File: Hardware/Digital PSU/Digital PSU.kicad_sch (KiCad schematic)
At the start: 35 parts, among them J1 ACin, J2 Relay power, J3 Conn_02x09, Q1 NJW0302, Q2 MJE15030, U1 LM334Z

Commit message: More work on PSU
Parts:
- R3: footprint Resistor_THT:R_Axial_DIN0207_L6.3mm_D2.5mm_P10.16mm_Horizontal -> Potentiometer_THT:Potentiometer_Bourns_3296W_Vertical; symbol Device:R_Variable -> Device:R_Potentiometer
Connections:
- net GND: now also R3.1; no longer R3.2
- net at D15.1 (K), J3.10 (Pin_10), J3.12 (Pin_12)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: now also R3.2, R3.3; no longer R3.1
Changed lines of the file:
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@@
+	(wire
+		(pts
+			(xy 102.616 153.162) (xy 96.012 153.162)
+		)
+		(stroke
+			(width 0)
+			(type default)
+		)
+	)
 	(wire
 		(pts
@@
 	(wire
 		(pts
+			(xy 96.012 153.162) (xy 96.012 158.496)
+		)
+		(stroke
+			(width 0)
+			(type default)
+		)
+	)
+	(wire
+		(pts
 			(xy 82.55 164.592) (xy 102.616 164.592)
 		)
@@
 		(pts
 			(xy 184.658 89.662) (xy 184.658 84.582)
+		)
+		(stroke
+			(width 0)
+			(type default)
+		)
+	)
+	(wire
+		(pts
+			(xy 96.012 158.496) (xy 98.806 158.496)
 		)
 		(stroke
@@
 	)
 	(symbol
-		(lib_id "Device:R_Variable")
-		(at 102.616 158.496 0)
+		(lib_id "Device:R_Potentiometer")
+		(at 102.616 158.496 180)
 		(unit 1)
 		(exclude_from_sim no)
@@
 		(fields_autoplaced yes)
 		(property "Reference" "R3"
-			(at 105.791 157.2838 0)
-			(effects
-				(font
-					(size 1.27 1.27)
-				)
-				(justify left)
+			(at 104.394 157.2838 0)
+			(effects
+				(font
+					(size 1.27 1.27)
+				)
+				(justify right)
 			)
 		)
 		(property "Value" "500R"
-			(at 105.791 159.7081 0)
-			(effects
-				(font
-					(size 1.27 1.27)
-				)
-				(justify left)
-			)
-		)
-		(property "Footprint" "Resistor_THT:R_Axial_DIN0207_L6.3mm_D2.5mm_P10.16mm_Horizontal"
-			(at 100.838 158.496 90)
+			(at 104.394 159.7081 0)
+			(effects
+				(font
+					(size 1.27 1.27)
+				)
+				(justify right)
+			)
+		)
+		(property "Footprint" "Potentiometer_THT:Potentiometer_Bourns_3296W_Vertical"
+			(at 102.616 158.496 0)
 			(effects
 				(font
@@
 			)
 		)
-		(property "Description" "Variable resistor"
+		(property "Description" "Potentiometer"
 			(at 102.616 158.496 0)
 			(effects
@@
 		(pin "1"
 		)
-		(instances
+		(pin "3"
+		)
+		(instances

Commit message: Added transformer for Digital PSU
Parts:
- added F2: Fuse - 8A T, ThePreAmp_PSU_Fuseholder:Keystone fuseholder 4527, symbol Device:Fuse
- added J4: 15V AC, THE_PREAMP_CONN_POWER_5_08:TBP01R1-508-02BK, symbol Connector:Conn_01x02_Socket
- added J5: 230V AC, THE_PREAMP_CONN_POWER_5_08:TBP01R1-508-02BK, symbol Connector:Conn_01x02_Socket
- added TR1: Hahn BV EL 603 1027, Transformer_Hahn_BV_EL_603_1027:Transformer_Hahn_BV_EL_603_1027, symbol Transformer_Hahn_BV_EL_603_1027:Hahn_BV_EL_603_1027
- J1: value ACin -> AC in
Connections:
- new net: F2.1, J5.1 (Pin_1)
- new net: J5.2 (Pin_2), TR1.7
- new net: J4.1 (Pin_1), TR1.9
- new net: J4.2 (Pin_2), TR1.13
- new net: F2.2, TR1.1

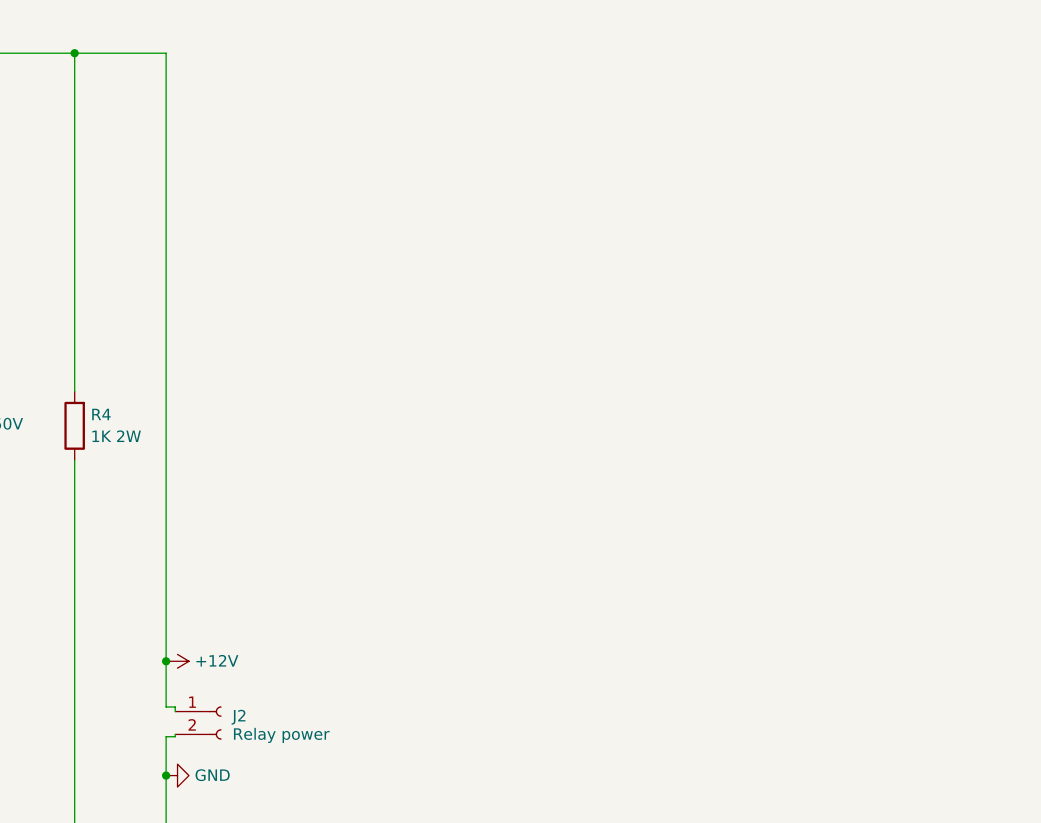
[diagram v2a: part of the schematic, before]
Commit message: Added LD1117V33 to digital psu
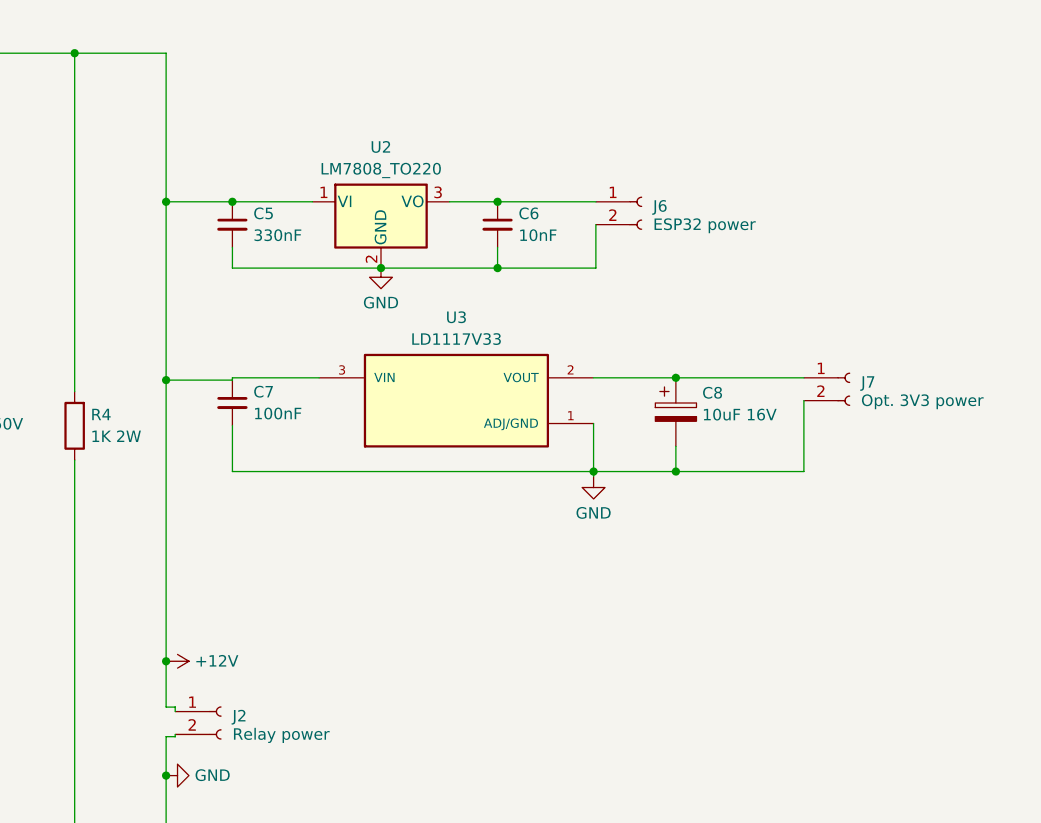
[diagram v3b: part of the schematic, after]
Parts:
- added C5: 330nF, symbol Device:C_Small
- added C6: 10nF, symbol Device:C_Small
- added C7: 100nF, symbol Device:C_Small
- added C8: 10uF 16V, Capacitor_THT:CP_Radial_D10.0mm_P5.00mm, symbol Device:C_Polarized
- added J6: ESP32 power, THE_PREAMP_CONN_POWER_5_08:TBP01R1-508-02BK, symbol Connector:Conn_01x02_Socket
- added J7: Opt. 3V3 power, THE_PREAMP_CONN_POWER_5_08:TBP01R1-508-02BK, symbol Connector:Conn_01x02_Socket
- added U2: LM7808_TO220, Package_TO_SOT_THT:TO-220-3_Vertical, symbol Regulator_Linear:LM7808_TO220
- added U3: LD1117V33, LD1117V33:TO255P1020X450X1968-3, symbol LD1117V33:LD1117V33
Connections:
- net +12V: now also C5.1, C7.1, U2.1 (VI), U3.3 (VIN)
- net GND: now also C5.2, C6.2, C7.2, C8.2, J6.2 (Pin_2), J7.2 (Pin_2), U2.2 (GND), U3.1 (ADJ/GND)
- new net: C8.1, J7.1 (Pin_1), U3.2 (VOUT)
- new net: C6.1, J6.1 (Pin_1), U2.3 (VO)

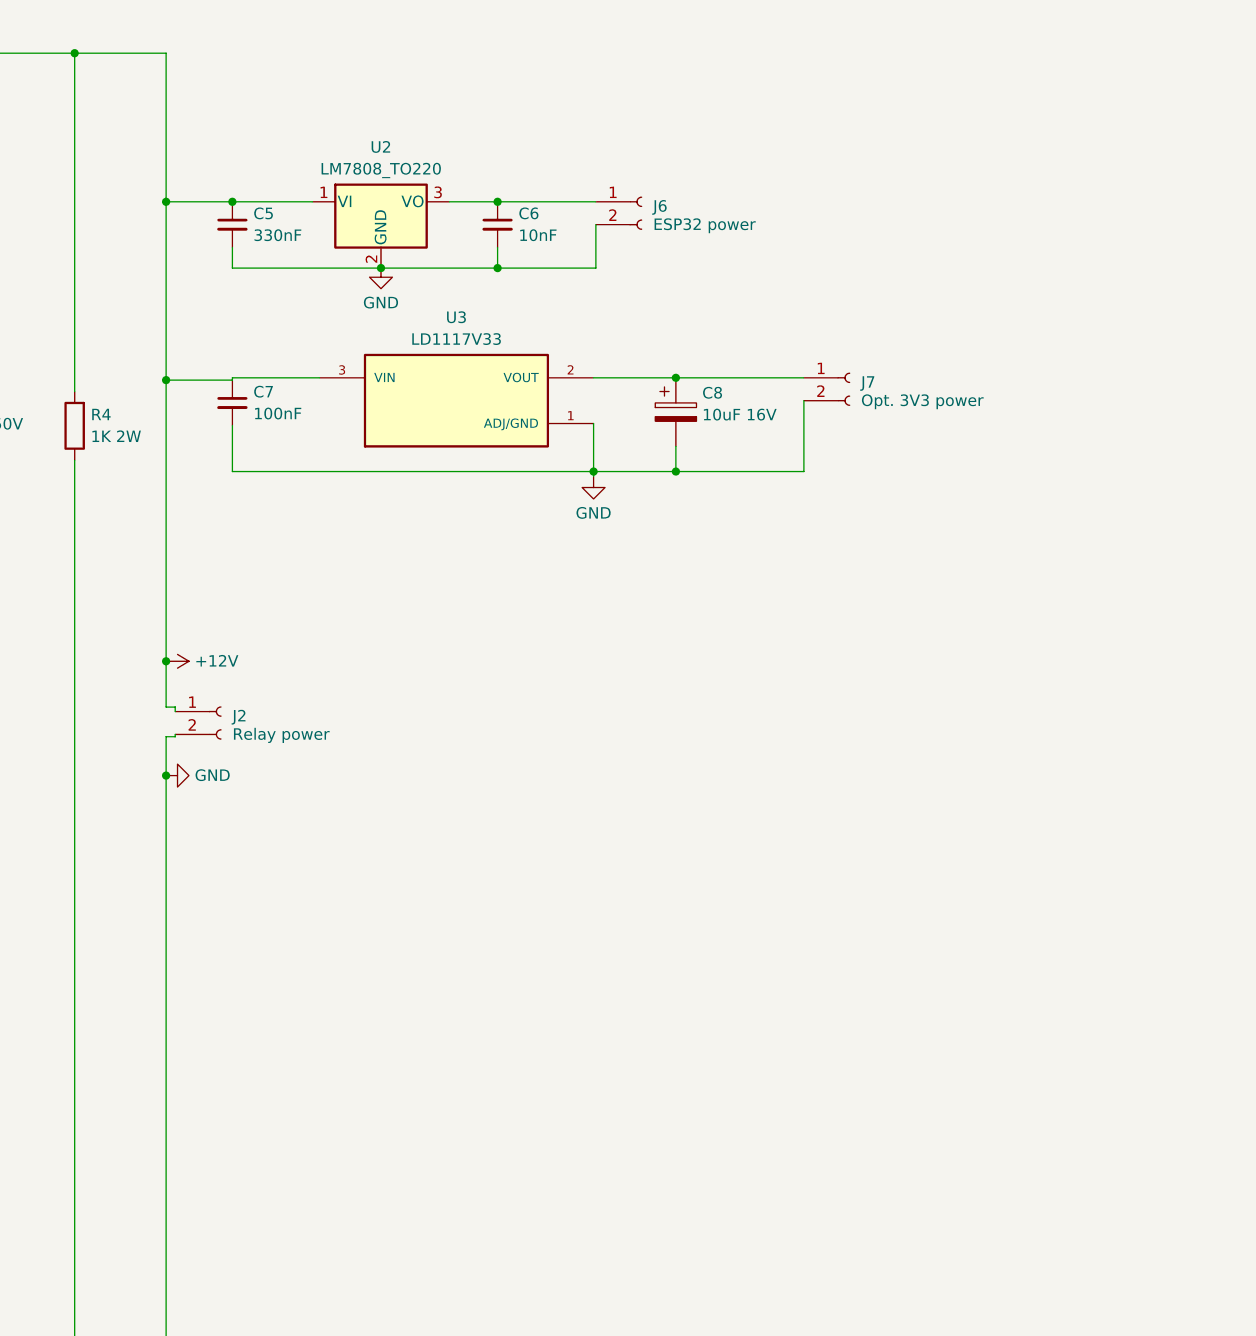
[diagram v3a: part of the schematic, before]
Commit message: Pcb dimensions
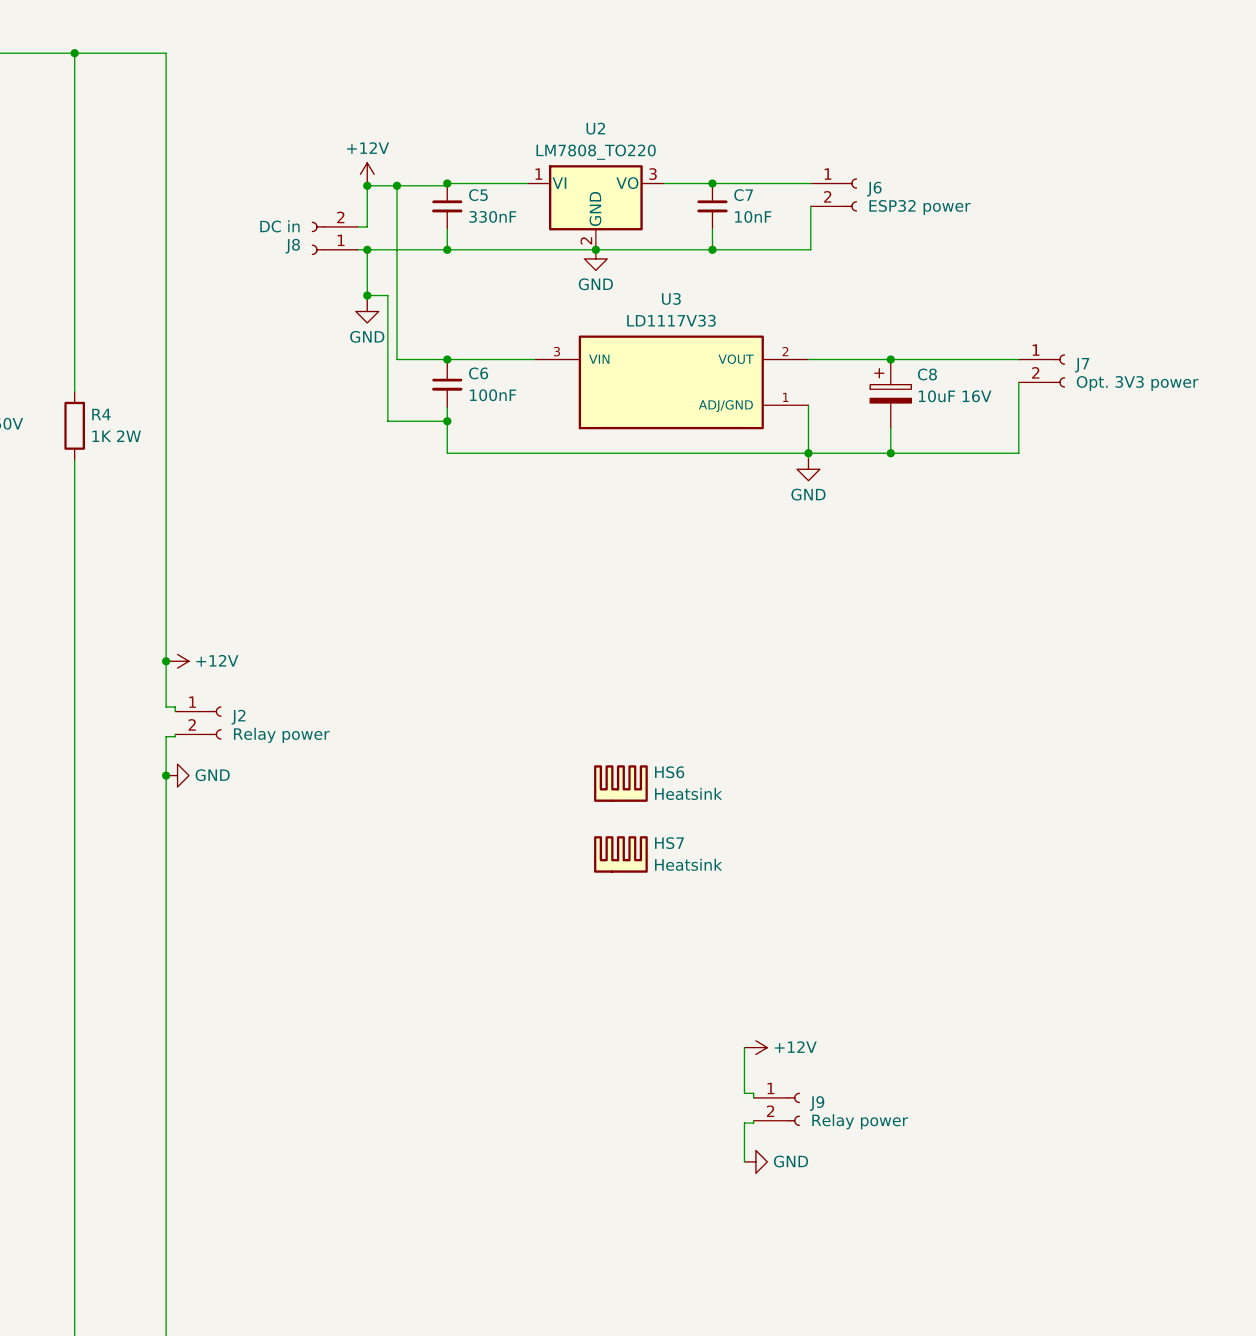
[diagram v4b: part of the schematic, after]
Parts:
- added HS6, HS7: Heatsink, ThePreAmp_PSU_Heatsinks:Heatsink_Fischer_SK145-STS_29x12mm_2xDrill2.5mm, symbol Mechanical:Heatsink
- added J8: DC in, THE_PREAMP_CONN_POWER_5_08:TBP01R1-508-02BK, symbol Connector:Conn_01x02_Socket
- added J9: Relay power, THE_PREAMP_CONN_POWER_5_08:TBP01R1-508-02BK, symbol Connector:Conn_01x02_Socket
- C5: footprint (none) -> Capacitor_SMD:C_0805_2012Metric_Pad1.18x1.45mm_HandSolder
- C6: value 10nF -> 100nF; footprint (none) -> Capacitor_SMD:C_0805_2012Metric_Pad1.18x1.45mm_HandSolder
- C7: value 100nF -> 10nF; footprint (none) -> Capacitor_SMD:C_0805_2012Metric_Pad1.18x1.45mm_HandSolder
- C8: footprint Capacitor_THT:CP_Radial_D10.0mm_P5.00mm -> Capacitor_SMD:C_1206_3216Metric_Pad1.33x1.80mm_HandSolder
- U3: footprint LD1117V33:TO255P1020X450X1968-3 -> Package_TO_SOT_THT:TO-220-3_Vertical
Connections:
- net +12V: now also C6.1, J8.2 (Pin_2), J9.1 (Pin_1); no longer C7.1
- net GND: now also J8.1 (Pin_1), J9.2 (Pin_2)
- net at J6.1 (Pin_1), U2.3 (VO): now also C7.1; no longer C6.1

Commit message: Small adjustments to draft
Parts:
- added H1, H10, H11, H12, H2, H3, H4, H5, H6, H7, H8, H9: MountingHole, MountingHole:MountingHole_3.2mm_M3_DIN965, symbol Mechanical:MountingHole
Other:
- moved on the sheet: HS6, HS7, J9
